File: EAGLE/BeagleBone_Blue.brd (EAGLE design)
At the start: 86.4 x 54.6 mm, 302 parts, among them J2 STRAWSON_EAGLE_LIB_SERVO_HEAD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, M1 JST_ZH_2, M2 JST_ZH_2, M3 JST_ZH_2, M4 JST_ZH_2, Q1 MOSFET-N, U1 TCAN1051HV, U10 TXS0108ERGYR, U13 EMMC, U2 SN74LV1T126DBVR, U3 TPD4S012DRY, U4 TPD4S012DRY, U5 24LC_32AT-I/OT, U6 SN74LVC1G07_DCK_5, U7 WL1835MODGBMOCT, U8 TPS2105_DBV_5, U9 TXS0108ERGYR, X2 SCHA5B0200, X3 USB1, X4 10118192-0001LF, Y1 24 MHz, Y2 32.768kHz

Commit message: Updated layout.
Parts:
- moved FUD5 2.16 mm to (74.7, -3.56)
- moved C28 0.59 mm to (21.0, -36.9)
- moved R2 0.30 mm to (23.7, -36.2)
- moved R58 0.30 mm to (20.3, -33.1)
- moved U5 0.30 mm to (20.9, -35.0)
- moved R23 0.30 mm to (23.7, -33.8)
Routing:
- net MDIR_2B: track 69.7 -> 38.4 mm, vias 3 -> 2
- net UART5_TX: track 71.8 -> 40.7 mm, vias 3 -> 2
- net SYS_5V: track 1.27 -> 21.2 mm
- net WIFI_LED: track 0.00 -> 11.0 mm
- net GND: track 219.1 -> 230.0 mm, vias 208 -> 211
- net GPIO3_17: track 10.5 -> 0.00 mm
- net SPI1_SS1: track 22.0 -> 11.9 mm, vias 2 -> 1
- net SPI1_SS2: track 15.6 -> 7.05 mm, vias 2 -> 1
- net LED_GRN: track 64.5 -> 73.0 mm, vias 4 -> 3
- net LED_RED: track 62.9 -> 71.1 mm, vias 4 -> 3
- net 3.3V: track 127.2 -> 132.5 mm
- net USB1_D_P: track 53.3 -> 48.4 mm
- net USB1_D_N: track 53.3 -> 48.9 mm
- net N$129: track 35.4 -> 31.5 mm
- net VCC: track 165.3 -> 162.7 mm
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
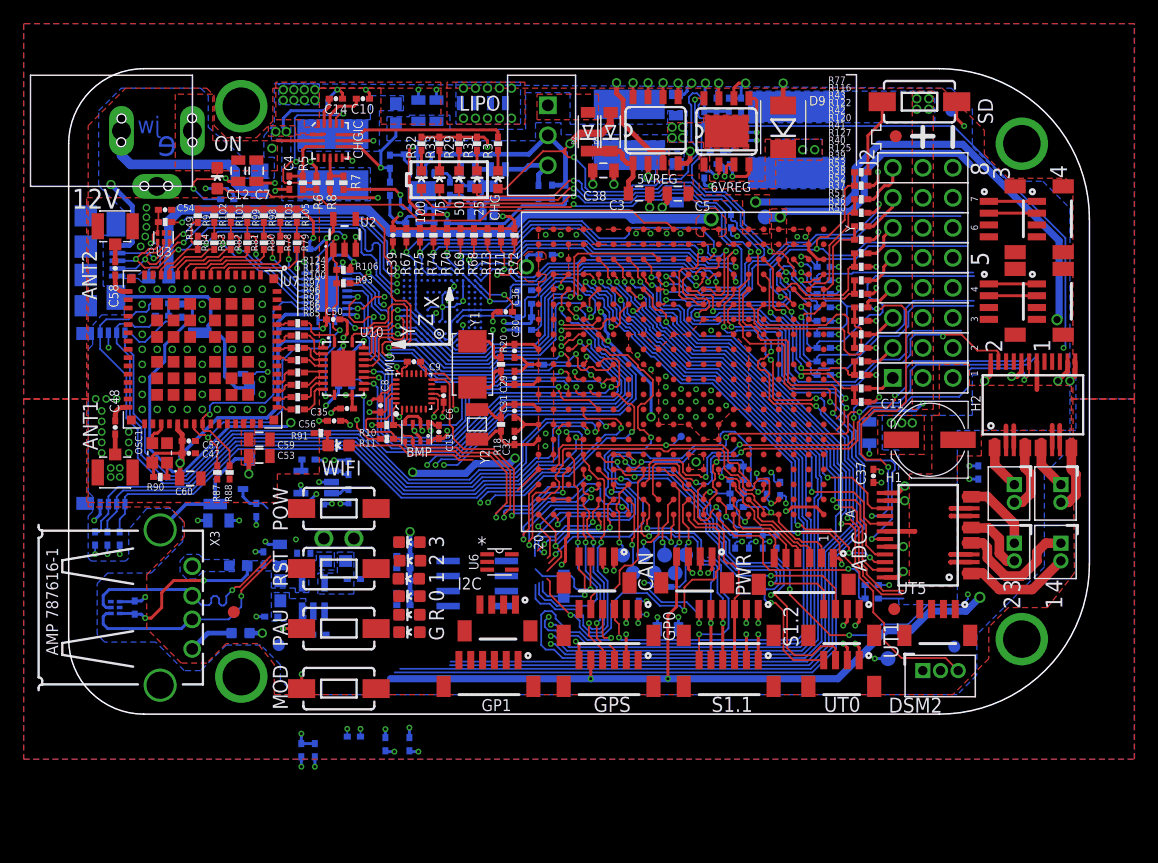
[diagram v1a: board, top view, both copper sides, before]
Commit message: Fixed L4, L5 DFM issues; Updated layout.
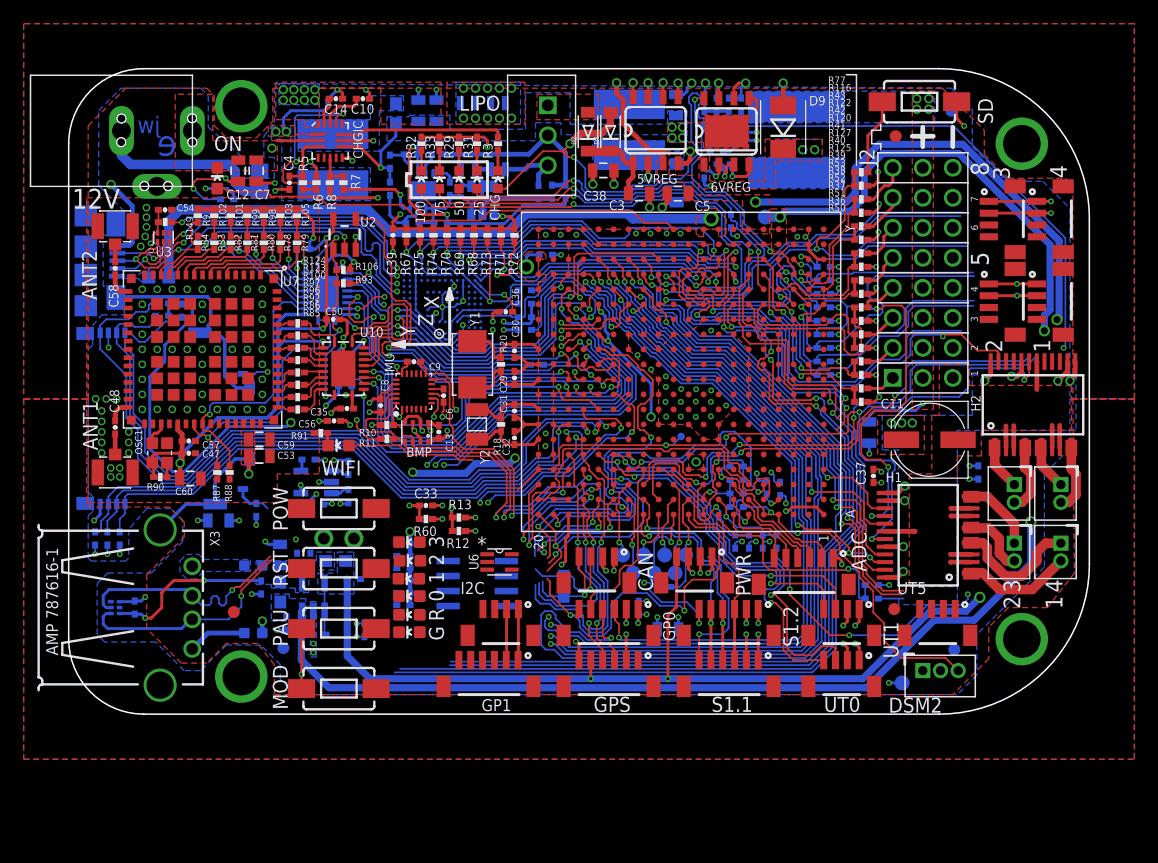
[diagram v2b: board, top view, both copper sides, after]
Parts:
- moved C33 23.2 mm to (30.2, -37.0), flipped to the top, turned to 0 degrees
- moved R60 21.7 mm to (30.2, -38.1), flipped to the top, turned to 0 degrees
- moved R13 19.6 mm to (33.0, -38.0), flipped to the top, turned to 0 degrees
- moved R12 19.1 mm to (33.0, -39.1), flipped to the top, turned to 180 degrees
- moved C27 9.06 mm to (25.0, -47.5), turned to 270 degrees
- moved C45 2.46 mm to (16.3, -43.9), turned to 270 degrees
- moved TP12 2.38 mm to (70.5, -52.0)
- moved C62 1.39 mm to (18.4, -46.9), turned to 270 degrees
- moved L5 1.27 mm to (15.6, -42.0)
- moved L4 1.08 mm to (15.6, -47.8)
- moved FUD6 0.46 mm to (18.2, -49.0)
- moved I2C 0.46 mm to (37.6, -47.0)
- moved FUD4 0.25 mm to (74.9, -49.1)
- moved R121 0.10 mm to (17.9, -44.3)
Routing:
- net SYS_5V: track 21.2 -> 130.8 mm, vias 1 -> 3
- net 5.0V: track 143.6 -> 159.0 mm
- net GND: track 230.0 -> 237.9 mm, vias 211 -> 214
- net 3.3V: track 132.5 -> 138.3 mm, vias 58 -> 59
- net N$128: track 3.88 -> 4.96 mm

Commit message: Updated layout.
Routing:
- net PRU_E_B: track 40.5 -> 11.2 mm, vias 2 -> 1
- net PRU_E_A: track 41.1 -> 12.3 mm, vias 2 -> 1
- net MDIR_2B: track 38.4 -> 48.4 mm
- net UART5_RX: track 39.3 -> 33.2 mm, vias 4 -> 2
- net UART5_TX: track 40.7 -> 45.6 mm, vias 2 -> 1
- net GND: track 237.9 -> 239.9 mm, vias 214 -> 215
- net 3.3V: track 138.3 -> 140.2 mm, vias 59 -> 60
- net MOT_STBY: track 56.8 -> 55.6 mm

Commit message: Updated layout.
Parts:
- moved R135 1.14 mm to (63.9, -20.2)
- moved R140 1.14 mm to (63.9, -21.3)
- moved FUD3 0.13 mm to (69.8, -5.71)
- moved FUD2 0.13 mm to (69.8, -45.8)
- moved FUD1 0.13 mm to (14.0, -45.8)
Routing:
- net PRU_E_B: track 11.2 -> 39.6 mm, vias 1 -> 2
- net PRU_E_A: track 12.3 -> 40.2 mm, vias 1 -> 2
- net UART5_RX: track 33.2 -> 50.6 mm, vias 2 -> 4
- net MDIR_2B: track 48.4 -> 32.2 mm, vias 2 -> 4
- net PWM_2B: track 31.8 -> 47.1 mm, vias 1 -> 4
- net MDIR_4B: track 24.5 -> 38.4 mm, vias 1 -> 2
- net MDIR_4A: track 23.3 -> 35.3 mm, vias 1 -> 2
- net UART5_TX: track 45.6 -> 56.0 mm, vias 1 -> 2
- net MDIR_3A: track 24.4 -> 34.3 mm, vias 1 -> 2
- net MDIR_3B: track 30.6 -> 40.4 mm, vias 2 -> 3
- net EQEP_2B: track 29.9 -> 37.7 mm, vias 1 -> 2
- net EQEP_2A: track 30.2 -> 37.3 mm, vias 1 -> 2
- net EQEP_1A: track 16.1 -> 21.9 mm, vias 1 -> 2
- net EQEP_1B: track 17.0 -> 21.3 mm, vias 1 -> 2
- net EQEP_0A: track 43.8 -> 46.9 mm, vias 3 -> 4
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
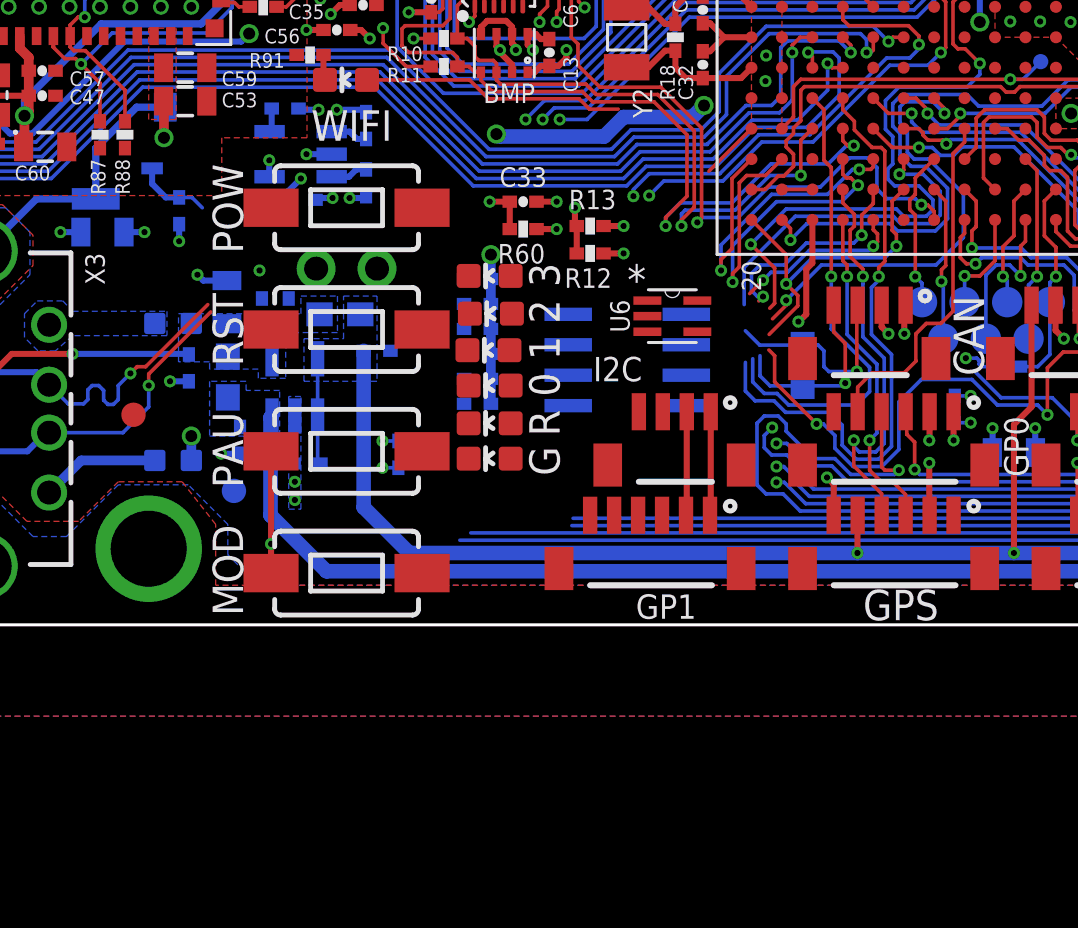
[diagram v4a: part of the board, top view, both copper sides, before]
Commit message: Updated button placement (preliminary).
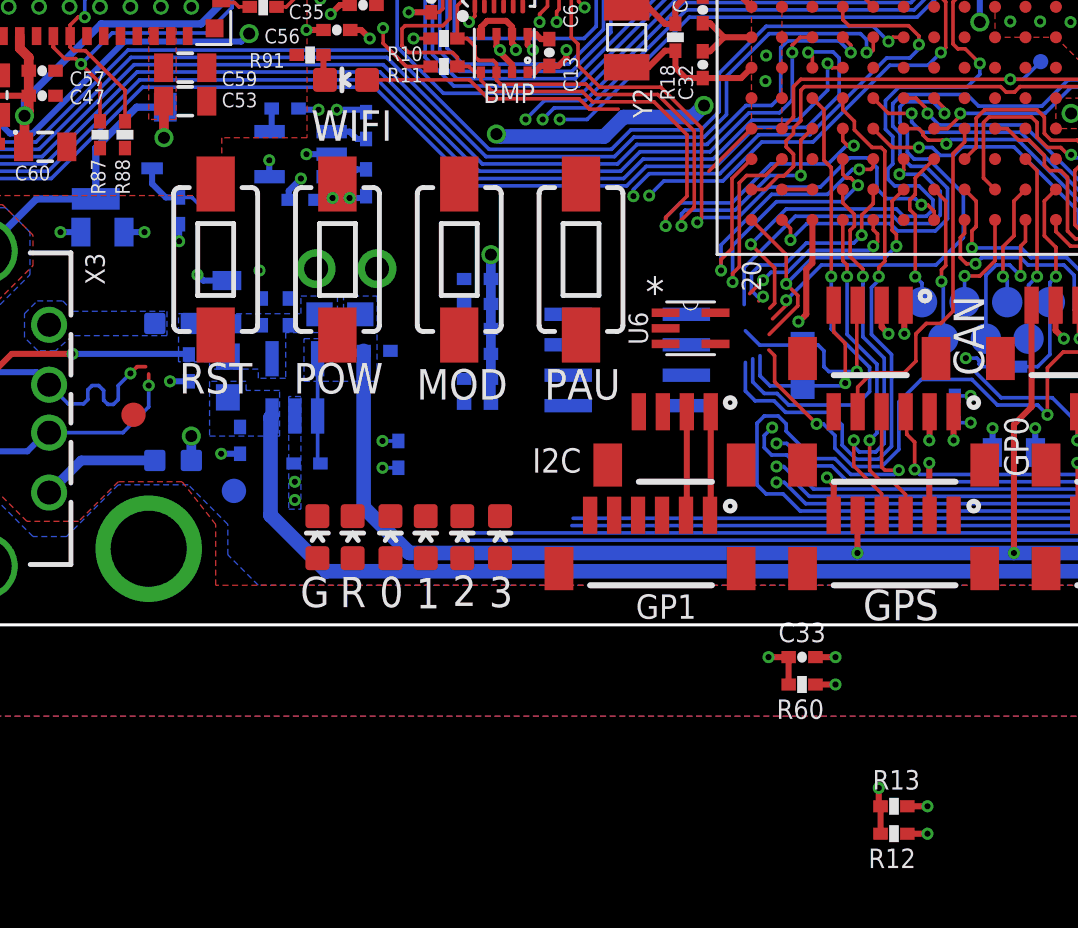
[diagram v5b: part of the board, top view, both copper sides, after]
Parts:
- moved R12 27.3 mm to (45.7, -63.3)
- moved R13 27.3 mm to (45.7, -62.2)
- moved C33 22.3 mm to (41.9, -56.0)
- moved R60 22.3 mm to (41.9, -57.1)
- moved MOD 13.9 mm to (27.6, -39.4), turned to 270 degrees
- moved PAU 12.6 mm to (32.6, -39.4), turned to 270 degrees
- moved 3 10.9 mm to (29.3, -51.0), turned to 0 degrees
- moved 2 9.40 mm to (27.7, -51.0), turned to 0 degrees
- moved 1 8.22 mm to (26.2, -51.0), turned to 0 degrees
- moved G 7.90 mm to (21.6, -51.0), turned to 0 degrees
- moved 0 7.56 mm to (24.7, -51.0), turned to 0 degrees
- moved R 7.43 mm to (23.1, -51.0), turned to 0 degrees
- moved RST 6.19 mm to (17.4, -39.4), turned to 90 degrees
- moved POW 2.19 mm to (22.5, -39.4), turned to 90 degrees
- moved U6 0.92 mm to (37.2, -42.2)
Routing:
- net GND: track 239.7 -> 234.6 mm, vias 215 -> 214
- net USB1_D_P: track 48.4 -> 44.7 mm
- net USB1_D_N: track 48.9 -> 45.3 mm

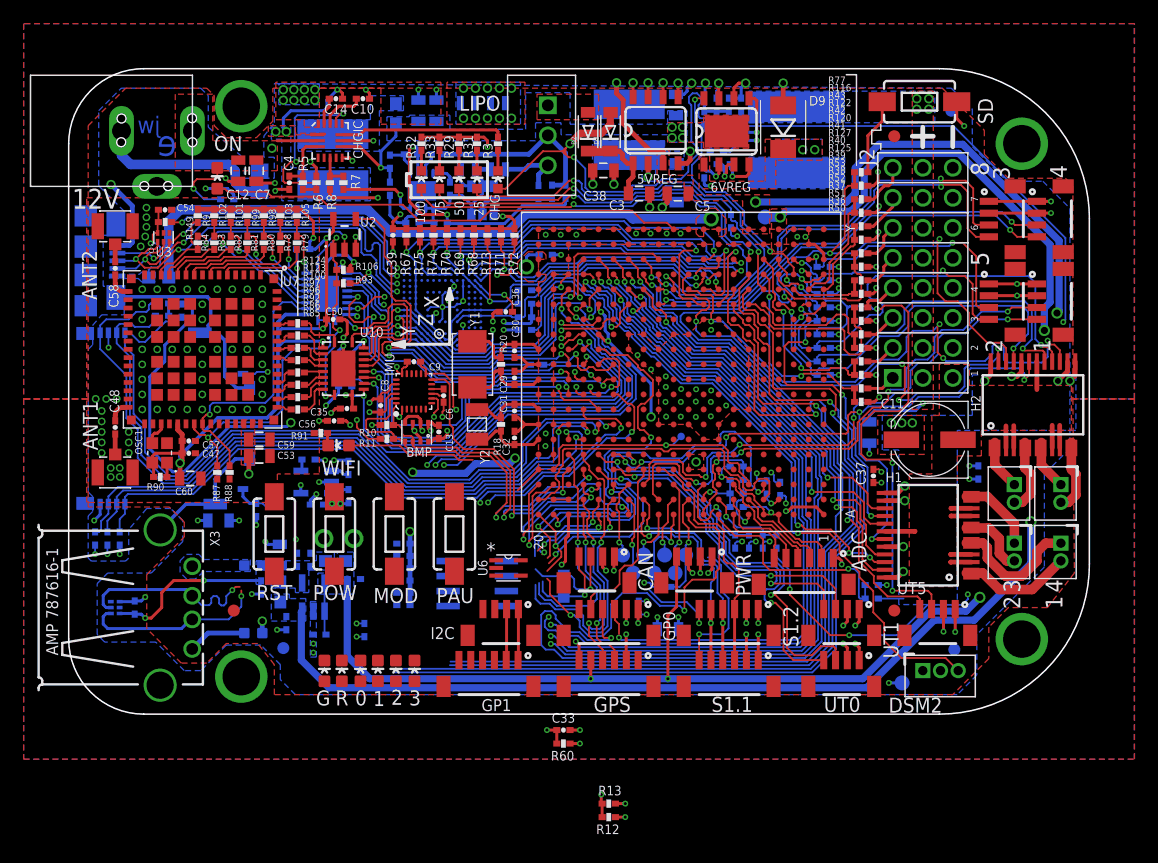
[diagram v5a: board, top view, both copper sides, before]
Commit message: Updated placement.
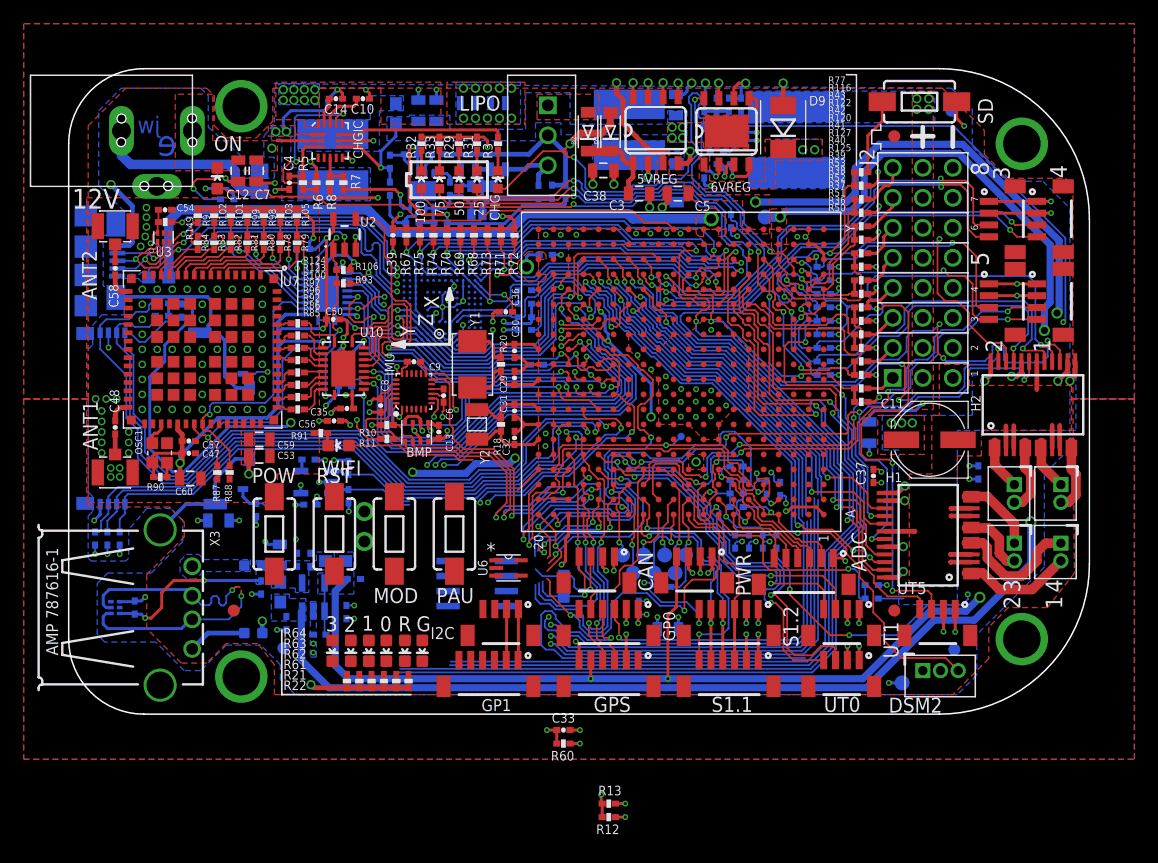
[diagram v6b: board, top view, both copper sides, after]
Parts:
- moved R64 12.6 mm to (23.5, -51.8), flipped to the top, turned to 90 degrees
- moved R63 11.2 mm to (24.6, -51.8), flipped to the top, turned to 90 degrees
- moved R62 9.92 mm to (25.6, -51.8), flipped to the top, turned to 90 degrees
- moved R61 8.67 mm to (26.7, -51.8), flipped to the top, turned to 90 degrees
- moved G 8.45 mm to (29.9, -49.3), turned to 180 degrees
- moved R21 7.49 mm to (27.7, -51.8), flipped to the top, turned to 270 degrees
- moved 3 7.16 mm to (22.3, -49.3), turned to 180 degrees
- moved R22 6.44 mm to (28.8, -51.8), flipped to the top, turned to 270 degrees
- moved R 5.60 mm to (28.4, -49.3), turned to 180 degrees
- moved POW 5.08 mm to (17.4, -39.4), turned to 270 degrees
- moved RST 5.08 mm to (22.5, -39.4), turned to 270 degrees
- moved 2 4.17 mm to (23.9, -49.3), turned to 180 degrees
- moved WP 4.12 mm to (25.0, -37.5)
- moved 0 2.77 mm to (26.9, -49.3), turned to 180 degrees
- moved C27 2.16 mm to (23.5, -46.0), turned to 90 degrees
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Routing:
- net GPIO1_17: track 80.5 -> 66.6 mm
- net I2C0_SCL: track 15.8 -> 21.9 mm
- net I2C0_SDA: track 17.3 -> 23.0 mm
- net 5.0V: track 158.7 -> 160.6 mm
- net GND: track 234.6 -> 236.0 mm
- net 3.3V: track 140.3 -> 139.3 mm
- net USR_LED2: track 60.6 -> 60.0 mm
- net USR_LED3: track 66.1 -> 65.6 mm

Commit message: Updated layout.
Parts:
- moved R12 19.4 mm to (34.5, -47.5), flipped to the bottom, turned to 0 degrees
- moved R13 19.3 mm to (34.5, -46.4), flipped to the bottom, turned to 180 degrees
- moved C27 9.44 mm to (32.9, -47.1), turned to 270 degrees
- moved 3 7.67 mm to (30.0, -49.1)
- moved G 7.57 mm to (22.4, -49.1)
- moved U1 5.50 mm to (29.1, -43.2), turned to 90 degrees
- moved R22 5.21 mm to (23.5, -51.8)
- moved R64 5.21 mm to (28.8, -51.8)
- moved 2 4.57 mm to (28.4, -49.1)
- moved R 4.57 mm to (23.9, -49.1)
- moved R21 3.12 mm to (24.6, -51.8)
- moved R63 3.12 mm to (27.7, -51.8)
- moved 1 1.53 mm to (26.9, -49.1)
- moved 0 1.48 mm to (25.4, -49.1)
- moved R61 1.04 mm to (25.6, -51.8)
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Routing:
- net LED_GRN: track 75.1 -> 101.0 mm, vias 1 -> 2
- net LED_RED: track 68.9 -> 94.1 mm, vias 1 -> 2
- net USB1_D_P: track 44.7 -> 69.4 mm
- net USB1_D_N: track 45.3 -> 69.4 mm
- net N$129: track 31.5 -> 49.6 mm
- net USR_LED0: track 64.6 -> 81.4 mm
- net N$75: track 17.7 -> 33.7 mm
- net USR_LED1: track 62.8 -> 77.8 mm
- net USR_LED2: track 60.0 -> 74.5 mm
- net POWER_BTN: track 2.51 -> 14.4 mm, vias 0 -> 1
- net USR_LED3: track 65.6 -> 76.0 mm
- net N$28: track 1.06 -> 11.5 mm
- net MODE_BTN: track 78.9 -> 88.2 mm
- net PAUSE_BTN: track 76.5 -> 85.7 mm
- net GPIO3_2: track 19.0 -> 26.4 mm, vias 2 -> 3
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
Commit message: Updated layout.
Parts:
- moved R60 26.7 mm to (22.3, -38.9), flipped to the bottom, turned to 180 degrees
- moved C33 25.2 mm to (22.3, -40.0), flipped to the bottom, turned to 180 degrees
- moved TP5 2.61 mm to (49.5, -32.3)
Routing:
- net SPI1_SS1: track 11.9 -> 46.6 mm, vias 1 -> 2
- net GPIO3_2: track 26.4 -> 51.4 mm, vias 3 -> 4
- net GPIO3_1: track 26.1 -> 50.1 mm, vias 3 -> 4
- net WIFI_LED: track 11.0 -> 31.1 mm, vias 0 -> 2
- net POWER_BTN: track 14.4 -> 34.3 mm, vias 1 -> 2
- net PAUSE_BTN: track 85.7 -> 96.2 mm, vias 1 -> 2
- net N$75: track 33.7 -> 41.3 mm
- net MODE_BTN: track 88.2 -> 95.2 mm, vias 1 -> 2
- net I2C0_SDA: track 27.5 -> 31.4 mm
- net I2C0_SCL: track 26.6 -> 30.2 mm
- net I2C2_SCL: track 33.3 -> 30.0 mm
- net I2C2_SDA: track 26.6 -> 24.0 mm
- net PMIC_PGOOD: track 14.0 -> 16.6 mm
- net DCAN1_SILENT: track 34.5 -> 32.0 mm
- net RESET: track 28.4 -> 30.1 mm
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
